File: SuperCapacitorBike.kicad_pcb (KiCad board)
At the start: 2 copper layers, 110.5 x 119.5 mm, 87 parts, among them J1 1988804, J10 1988862, J11 Barrel_Jack_Switch, J13 1988862, J14 1988817, J2 GND, J3 RX, J4 TX, J5 RESET, J6 1988817, J7 1190363, J8 1190363, J9 1988862, K1 AWHSH105D00G, K2 AWHSH105D00G, Q1 IRFZ44N, Q2 IRFZ44N, Q3 IRFZ44N, Q4 IRFZ44N, Q5 IRFZ44N, Q6 IRFZ44N, Q7 GT065P06T, Q8 IRFZ44N, U1 IR2104, U10 L78L33_TO92, U2 IR2104, U3 IR2104, U4 UCC37324P, U5 MCP23017_SP, U6 ATmega328-P, U7 L7805, U8 ULN2003, U9 MCP4151-xxxx-P

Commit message: Major design improvements to prototyping PCB
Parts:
- removed D9: 1N5819, Diode_THT:D_DO-41_SOD81_P10.16mm_Horizontal
- removed L2: 10uH, Inductor_RLB0712_100KL:IND_BOURNS_RLB0712
- C9: value 100nF -> 0.1uF
- moved J13 42.6 mm to (27.3, 81.8), turned to -90 degrees
- moved J10 42.3 mm to (27.3, 39.5), turned to -90 degrees
- moved J9 42.2 mm to (82.1, 31.0), turned to 180 degrees
- moved R15 25.5 mm to (82.9, 101.5), turned to 0 degrees
- moved C9 21.6 mm to (90.5, 86.7)
- moved J14 19.8 mm to (126.9, 31.0), turned to 180 degrees
- moved J6 19.7 mm to (27.3, 123.9), turned to -90 degrees
- moved R12 10.2 mm to (77.3, 130.0), turned to -90 degrees
- moved D4 10.2 mm to (56.0, 75.9), turned to -90 degrees
- moved R7 10.1 mm to (82.3, 130.1), turned to -90 degrees
- moved J1 8.84 mm to (100.9, 33.8), turned to 180 degrees
- moved C14 5.10 mm to (50.0, 86.6), turned to 90 degrees
- moved C16 5.08 mm to (53.2, 90.4), turned to -90 degrees
- moved R16 4.95 mm to (108.3, 101.5)
- moved S1 3.01 mm to (50.5, 65.2)
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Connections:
- C1 pad 2: /Half bridge Circuit/VS -> P1
- C4 pad 2: /Half bridge Circuit/VS -> P2
- C6 pad 2: /Half bridge Circuit/VS -> P3
- C9 pad 1: Net-(U6-AVCC) -> +5V
- D11 pad 2: +12V -> +5V
- J1 pad 1: unconnected-(J1-Pad1) -> /Motor Controller/LED_1
- J1 pad 2: unconnected-(J1-Pad2) -> GND
- J6 pad 1: P1 -> P3
- J6 pad 2: P2 -> P1
- J6 pad 3: P3 -> P2
- J9 pad 2: MOSI -> Net-(D11-K)
- J9 pad 3: SS1 -> Net-(D12-K)
- J9 pad 4: /Motor Controller/DC -> /Motor Controller/RESET_DISPLAY
- J9 pad 5: /Motor Controller/RESET_DISPLAY -> /Motor Controller/DC
- J9 pad 6: Net-(D12-K) -> MOSI
- J9 pad 7: Net-(D11-K) -> SS1
- K2 pad 1: C1- -> GND
- R12 pad 1: /Half bridge Circuit/LO_3 -> Net-(U3-LO)
- R12 pad 2: Net-(U3-LO) -> /Half bridge Circuit/LO_3
- R7 pad 1: /Half bridge Circuit/HO_3 -> Net-(U3-HO)
- R7 pad 2: Net-(U3-HO) -> /Half bridge Circuit/HO_3
- U1 pad 6: /Half bridge Circuit/VS -> P1
- U2 pad 6: /Half bridge Circuit/VS -> P2
- U3 pad 6: /Half bridge Circuit/VS -> P3
- U6 pad 20: Net-(U6-AVCC) -> +5V
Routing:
- net +5V: track 6.64 -> 373.8 mm, vias 0 -> 9
- net +12V: track 48.9 -> 229.4 mm
- net SD: track 0.00 -> 156.1 mm, vias 0 -> 5
- net SS1: track 0.00 -> 149.5 mm, vias 0 -> 2
- net MOSI: track 0.00 -> 139.9 mm, vias 0 -> 3
- net +3.3V: track 0.00 -> 135.7 mm, vias 0 -> 1
- net SS2: track 0.00 -> 123.6 mm, vias 0 -> 2
- net /Motor Controller/HALL_A: track 0.00 -> 104.3 mm, vias 0 -> 3
- net SCK: track 0.00 -> 103.8 mm, vias 0 -> 2
- net C1+: track 0.00 -> 103.1 mm
- net RELAY_1: track 0.00 -> 90.7 mm, vias 0 -> 2
- net RELAY_2: track 0.00 -> 89.5 mm, vias 0 -> 1
- net /Motor Controller/HALL_C: track 0.00 -> 85.9 mm, vias 0 -> 1
- net /Motor Controller/TH_DATA: track 0.00 -> 85.1 mm, vias 0 -> 1
- net /Motor Controller/HALL_B: track 0.00 -> 76.1 mm, vias 0 -> 1
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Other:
- board text added: "*"
- board text added: "+VCC"
- board text added: "3.3V"
- board text added: "5V"
- board text added: "A"
- board text added: "B"
- board text added: "BRK1"
- board text added: "BRK2"
- board text added: "C"
- board text added: "C1+"
- board text added: "C2-"
- board text added: "DC"
- board text added: "Designed By: Andrew Fischer =)"
- board text added: "FAULT"
- board text added: "GND"
- board text added: "LED_1"
- board text added: "MOSI"
- board text added: "P1"
- board text added: "P2"
- board text added: "P3"
- board text added: "PWR"
- board text added: "RESET"
- board text added: "SCK"
- board text added: "SS1"
- board text added: "SW1"
- board text added: "SW2"
- board text added: "SW3"
- board text added: "SW4"
- board text added: "SuperCapBike Prototype Board"
- board text added: "TH"
- board text removed: "PWR_LED"

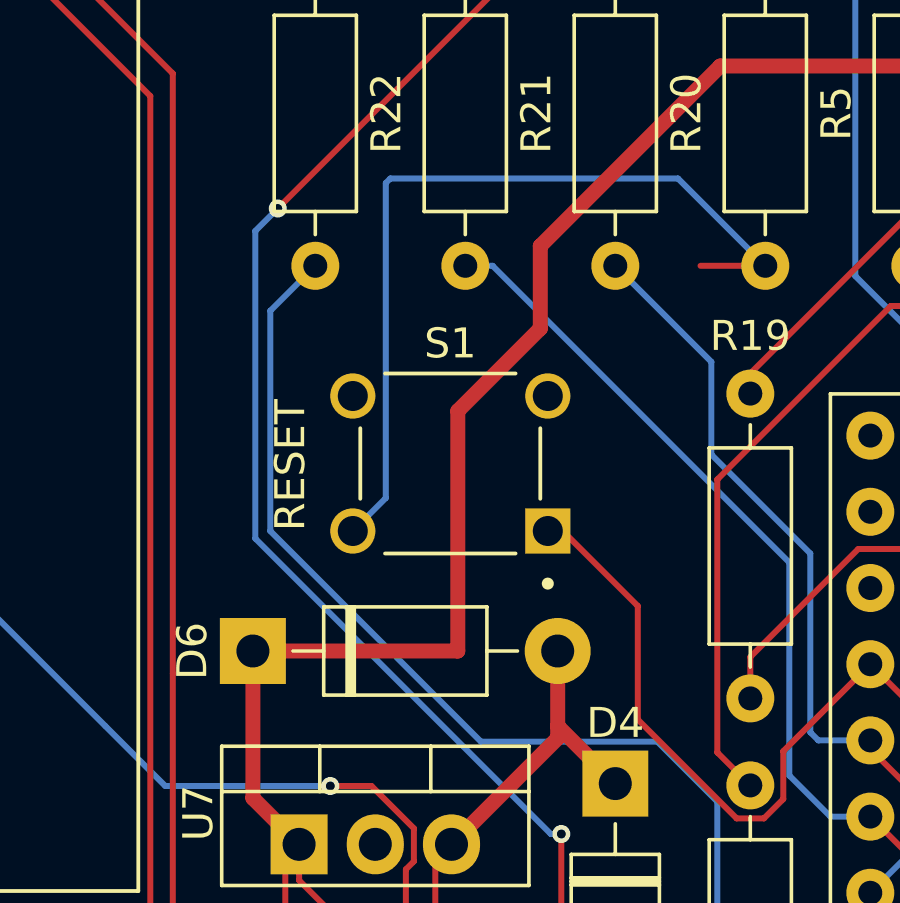
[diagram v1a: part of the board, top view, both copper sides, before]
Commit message: Added git ignore file
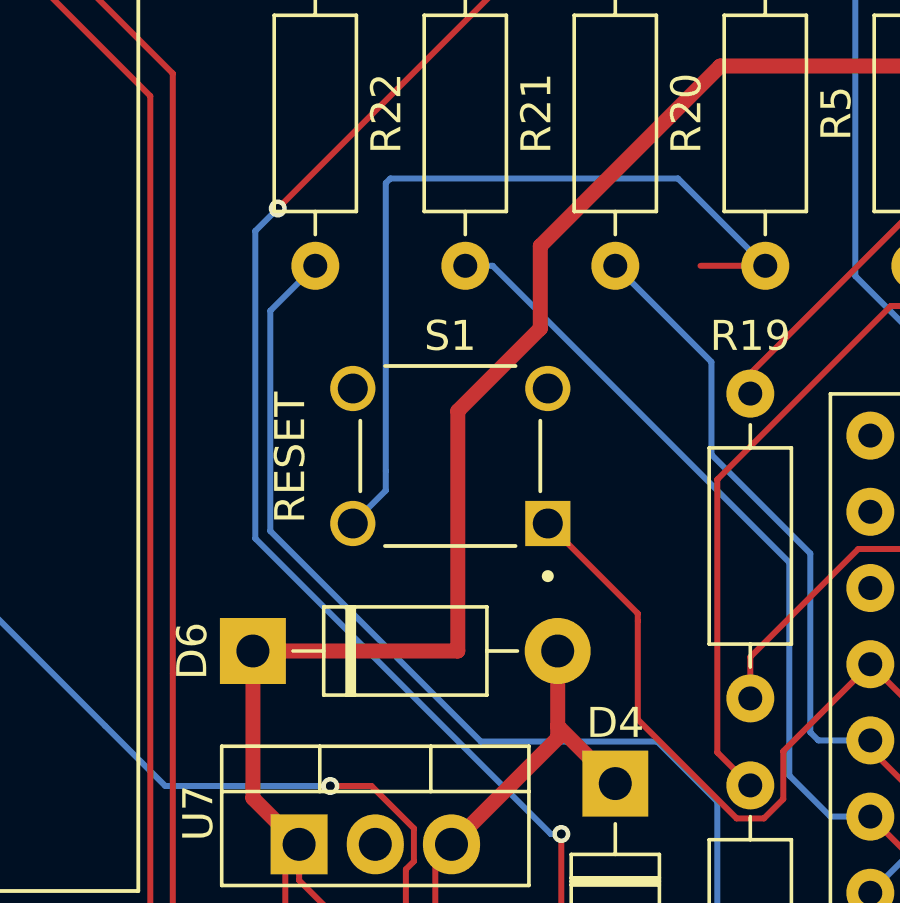
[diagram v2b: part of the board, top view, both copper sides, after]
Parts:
- moved S1 0.25 mm to (50.5, 65.0)
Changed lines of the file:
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@@
 	(footprint "TS02_66_50_BK_160_LCR_D:SW_TS02-66-50-BK-160-LCR-D"
 		(layer "F.Cu")
-		(at 50.5 65.25 180)
+		(at 50.5 65 180)
 		(property "Reference" "S1"
 			(at 0 4 0)
@@
 	)
 	(gr_text "RESET"
-		(at 45.75 67.5 90)
+		(at 45.75 67.25 90)
 		(layer "F.SilkS")
 		(effects
@@
 	)
 	(segment
+		(start 56.75 70.5)
+		(end 56.75 73.785635)
+		(width 0.2)
+		(layer "F.Cu")
+		(net 14)
+	)
+	(segment
 		(start 60.955635 77.08)
 		(end 61.6 76.435635)
@@
 	)
 	(segment
-		(start 69 75.7)
-		(end 71.5 73.2)
+		(start 53.75 67.25)
+		(end 56.75 70.25)
 		(width 0.2)
 		(layer "F.Cu")
@@
 	)
 	(segment
-		(start 71.5 73.2)
-		(end 72.8 73.2)
+		(start 56.75 70.25)
+		(end 56.75 70.5)
 		(width 0.2)
 		(layer "F.Cu")
@@
 	)
 	(segment
-		(start 60.044365 77.08)
-		(end 60.955635 77.08)
+		(start 69 75.7)
+		(end 71.5 73.2)
 		(width 0.2)
 		(layer "F.Cu")
@@
 	)
 	(segment
-		(start 61.6 74.84)
-		(end 64.5 71.94)
+		(start 71.5 73.2)
+		(end 72.8 73.2)
 		(width 0.2)
 		(layer "F.Cu")
@@
 	)
 	(segment
-		(start 56.75 70)
-		(end 56.75 73.785635)
+		(start 60.044365 77.08)
+		(end 60.955635 77.08)
 		(width 0.2)
 		(layer "F.Cu")
@@
 	)
 	(segment
-		(start 53.5 67.5)
-		(end 54.25 67.5)
+		(start 61.6 74.84)
+		(end 64.5 71.94)
 		(width 0.2)
 		(layer "F.Cu")
@@
 	)
 	(segment
-		(start 54.25 67.5)
-		(end 56.75 70)
+		(start 53.5 67.5)
+		(end 54.25 67.5)
 		(width 0.2)
 		(layer "F.Cu")
@@
 	)
 	(segment
-		(start 47.25 67.5)
-		(end 48.35 66.4)
+		(start 47.25 67.25)
+		(end 48.35 66.15)
+		(width 0.2)
+		(layer "B.Cu")
+		(net 43)
+	)
+	(segment
+		(start 48.35 65.5)
+		(end 48.35 55.9)
 		(width 0.2)
 		(layer "B.Cu")
@@
 	)
 	(segment
-		(start 48.35 66.4)
-		(end 48.35 55.9)
+		(start 48.35 66.15)
+		(end 48.35 65.5)
 		(width 0.2)
 		(layer "B.Cu")

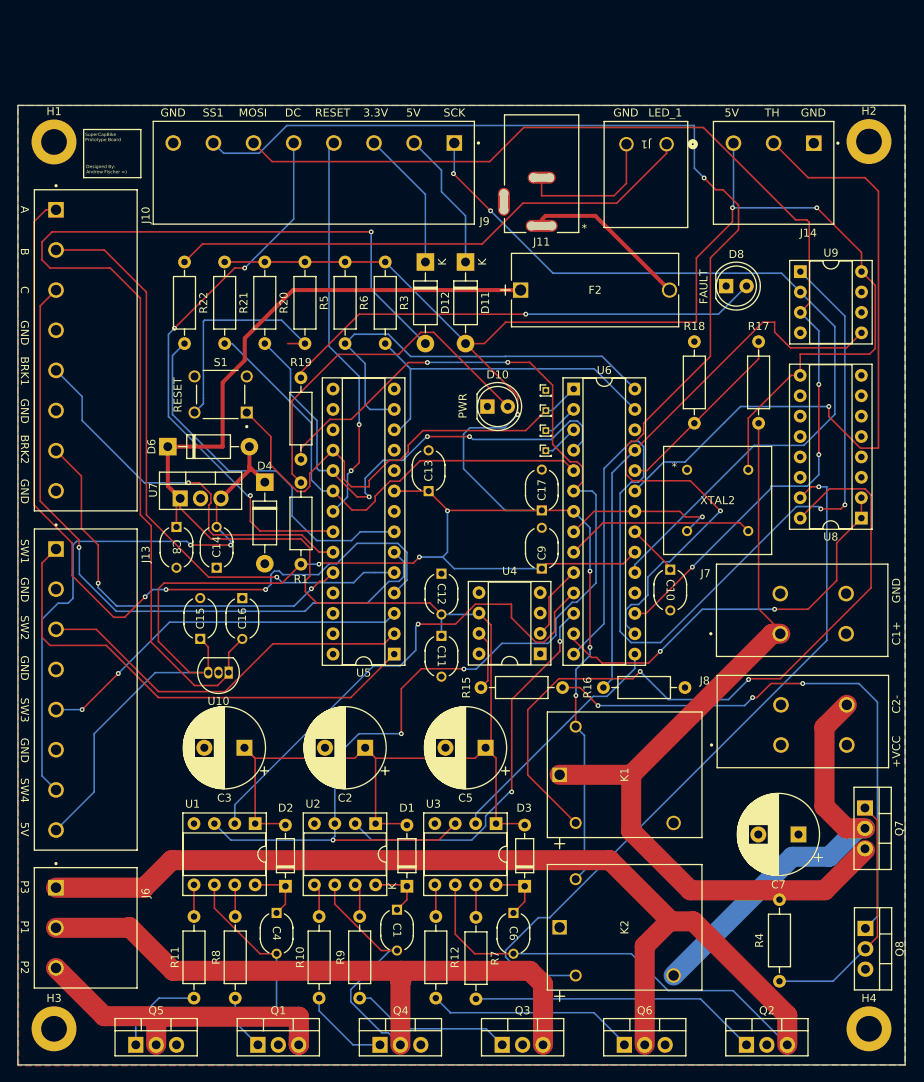
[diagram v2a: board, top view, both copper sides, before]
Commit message: Removed a couple redundent VIA's, added +5Vpin
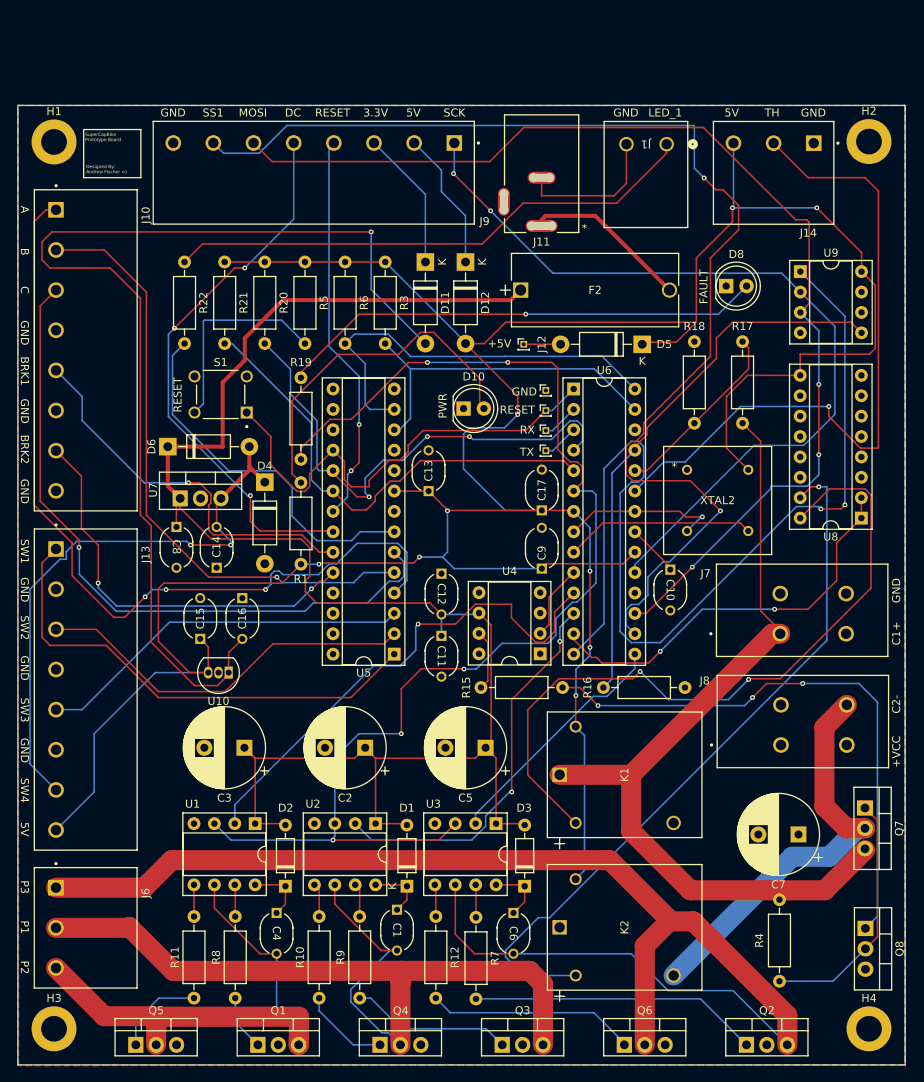
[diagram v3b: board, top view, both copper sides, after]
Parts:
- added D5: 1N5819, Diode_THT:D_DO-41_SOD81_P10.16mm_Horizontal, F.Cu at (103.0, 58.8)
- added J12: +5V, Connector_PinHeader_1.00mm:PinHeader_1x01_P1.00mm_Vertical, F.Cu at (88.2, 58.8)
- moved D11 5.00 mm to (76.0, 48.5)
- moved D12 5.00 mm to (81.0, 48.5)
- moved D10 2.99 mm to (80.8, 66.8)
- moved R17 2.00 mm to (115.5, 68.6)
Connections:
- D11 pad 2: +5V -> +3.3V
- D12 pad 2: +3.3V -> +5V
- J9 pad 2: Net-(D11-K) -> Net-(D12-K)
- J9 pad 3: Net-(D12-K) -> Net-(D11-K)
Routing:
- net +5V: track 373.8 -> 387.1 mm
- net Net-(D5-A): track 0.00 -> 4.59 mm
- net Net-(R5-Pad2): track 27.9 -> 25.7 mm
- net SD: track 156.1 -> 157.7 mm
- net Net-(D10-A): track 44.9 -> 43.9 mm
- net /Motor Controller/SW_4: track 71.6 -> 72.6 mm
- net C1+: track 103.1 -> 103.9 mm
- net /Motor Controller/SW_3: vias 2 -> 0
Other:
- board text added: "+5V"
- board text added: "RX"
- board text added: "TX"

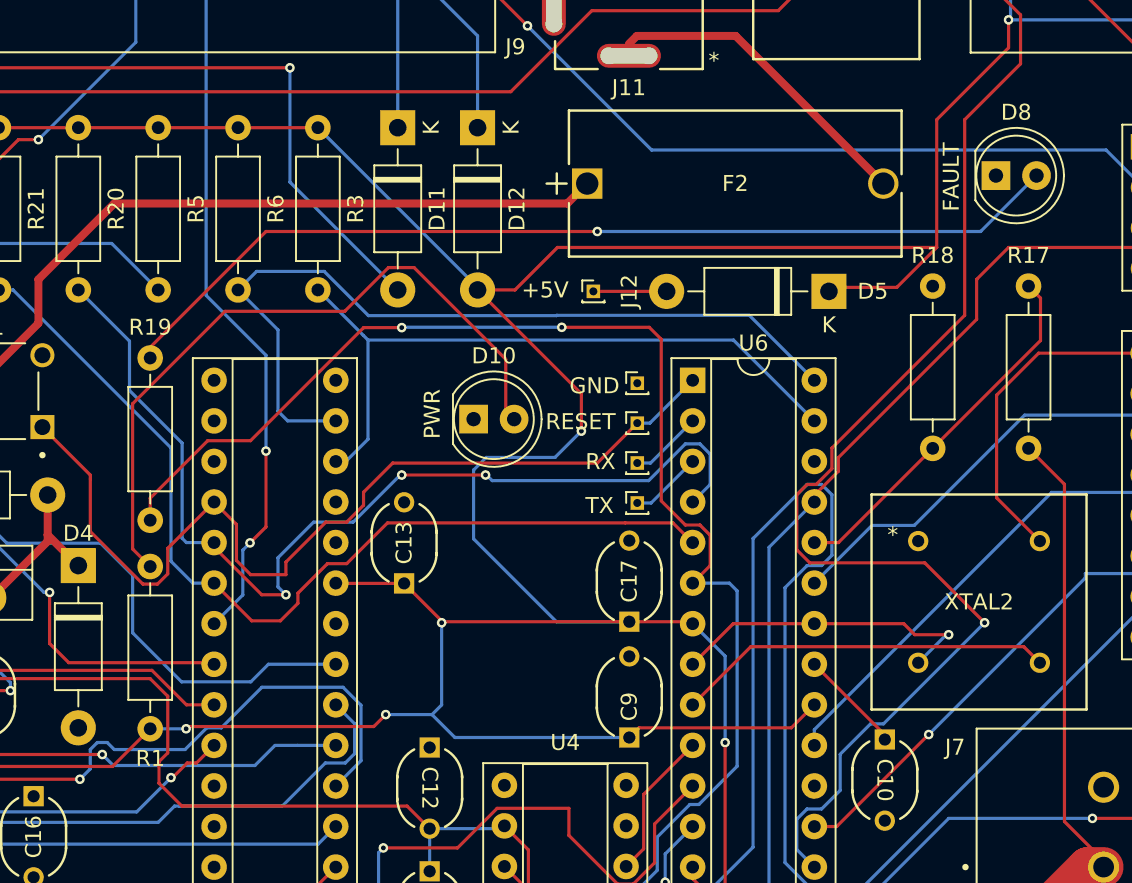
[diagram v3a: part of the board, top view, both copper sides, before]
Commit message: Fixed minor inconsistencies, improved orginization, MOSFET gate resistors calculted.
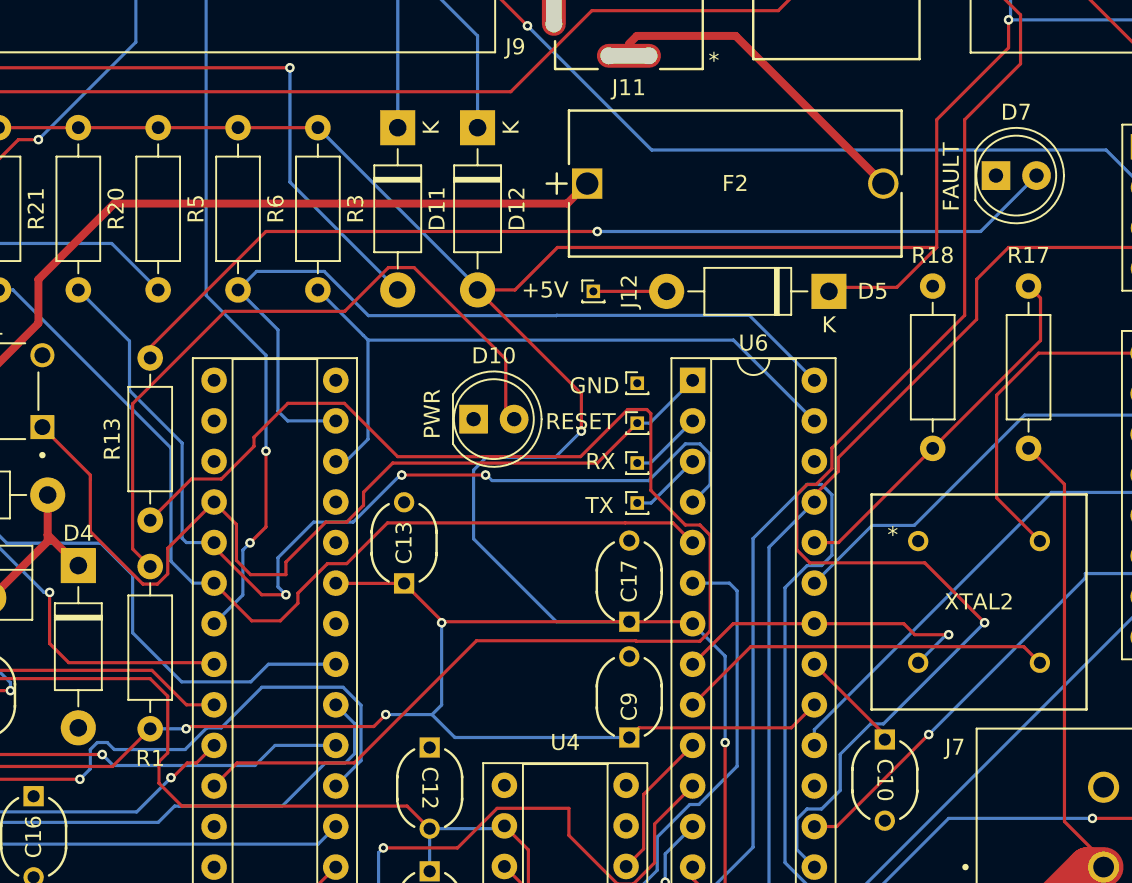
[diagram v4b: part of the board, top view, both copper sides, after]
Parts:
- removed D8: FAULT_LED, LED_THT:LED_D5.0mm
- removed R19: 220, Resistor_THT:R_Axial_DIN0207_L6.3mm_D2.5mm_P10.16mm_Horizontal
- added D7: FAULT_LED, LED_THT:LED_D5.0mm, F.Cu at (113.5, 51.5)
- added R13: 220Ω, Resistor_THT:R_Axial_DIN0207_L6.3mm_D2.5mm_P10.16mm_Horizontal, F.Cu at (60.5, 73.1)
- R1, R22: value 220 -> 220Ω
- R10, R11, R12, R15, R7, R8, R9: value R_US -> 47Ω
- R20, R21, R3, R5, R6: value 10k -> 10kΩ
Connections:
- net /Motor Controller/RELAYS renamed RELAYS
- U5 pad 25: unconnected-(U5-GPA4-Pad25) -> Net-(U5-GPA4)
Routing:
- net Net-(U5-GPA4): track 0.00 -> 88.2 mm
- net Net-(D8-A): track 60.6 -> 0.00 mm, vias 1 -> 0
- net Net-(D7-A): track 0.00 -> 60.6 mm, vias 0 -> 1
- net SD: track 157.7 -> 102.1 mm, vias 5 -> 3
